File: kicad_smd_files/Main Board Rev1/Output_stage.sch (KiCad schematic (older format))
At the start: 41 parts, among them J10 OUTPUT B, J9 OUTPUT A, Q3 DMN10H170SK3-13, Q4 DMP6180SK3-13, Q5 DMN10H170SK3-13, Q6 DMN10H170SK3-13, Q7 DMP6180SK3-13, Q8 DMN10H170SK3-13, U7 LM358N, U8 LTC1661

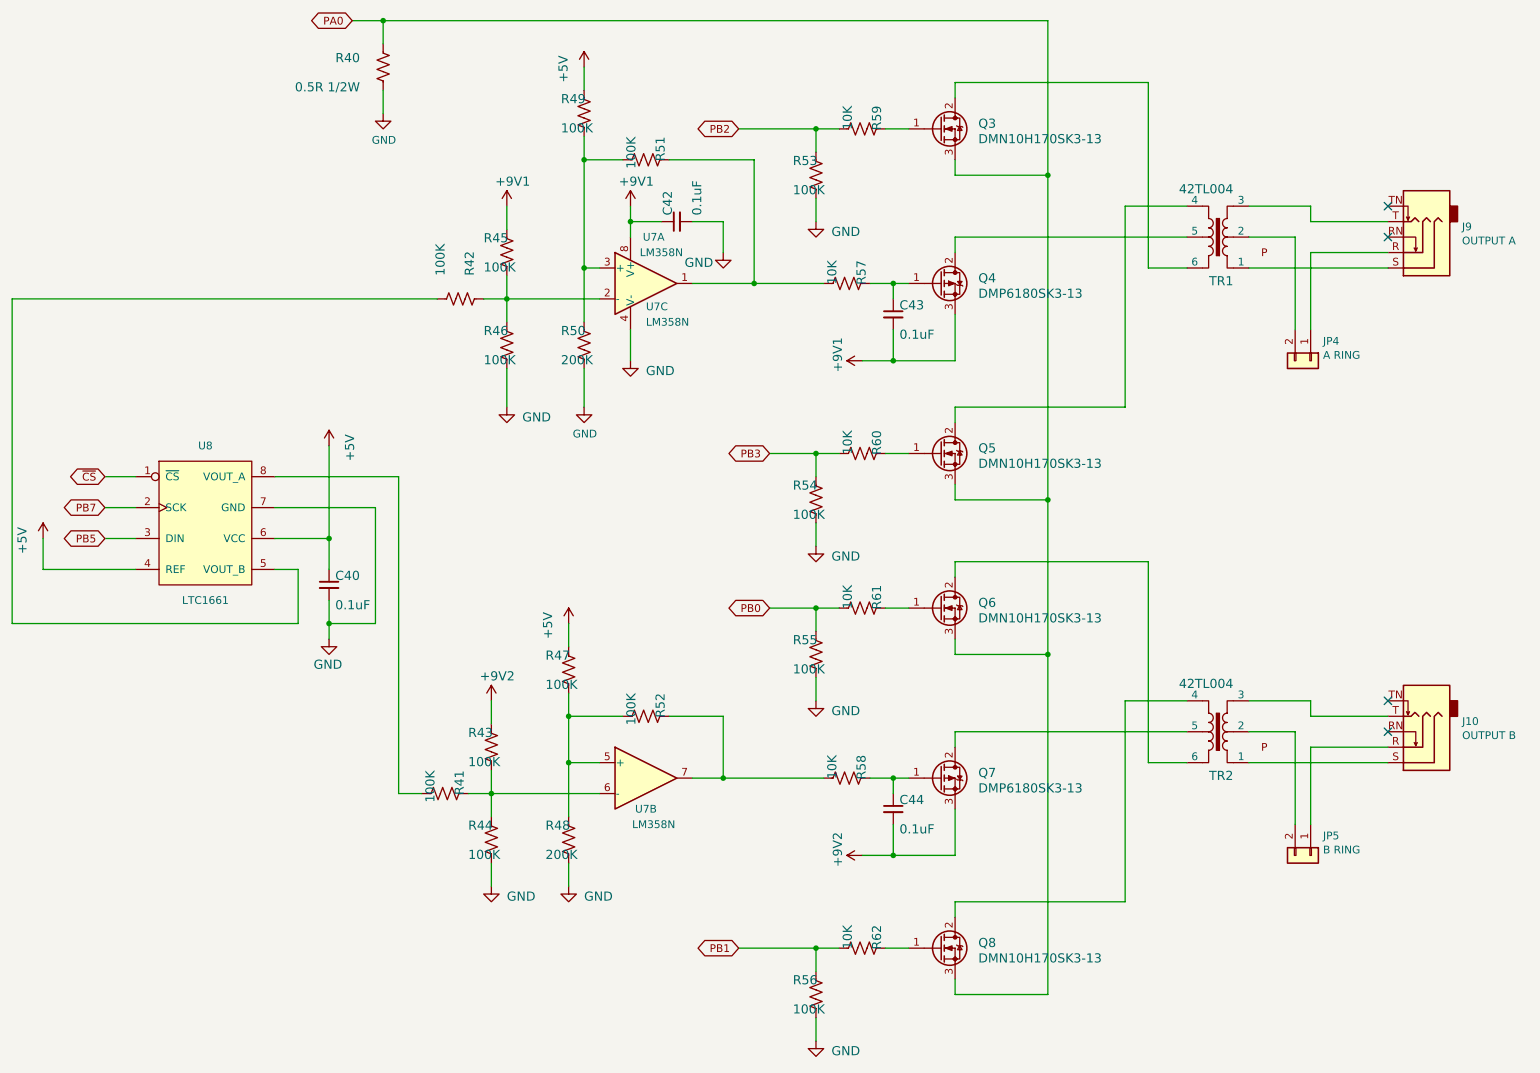
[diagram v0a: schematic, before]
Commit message: Smaller PCB, cheaper parts
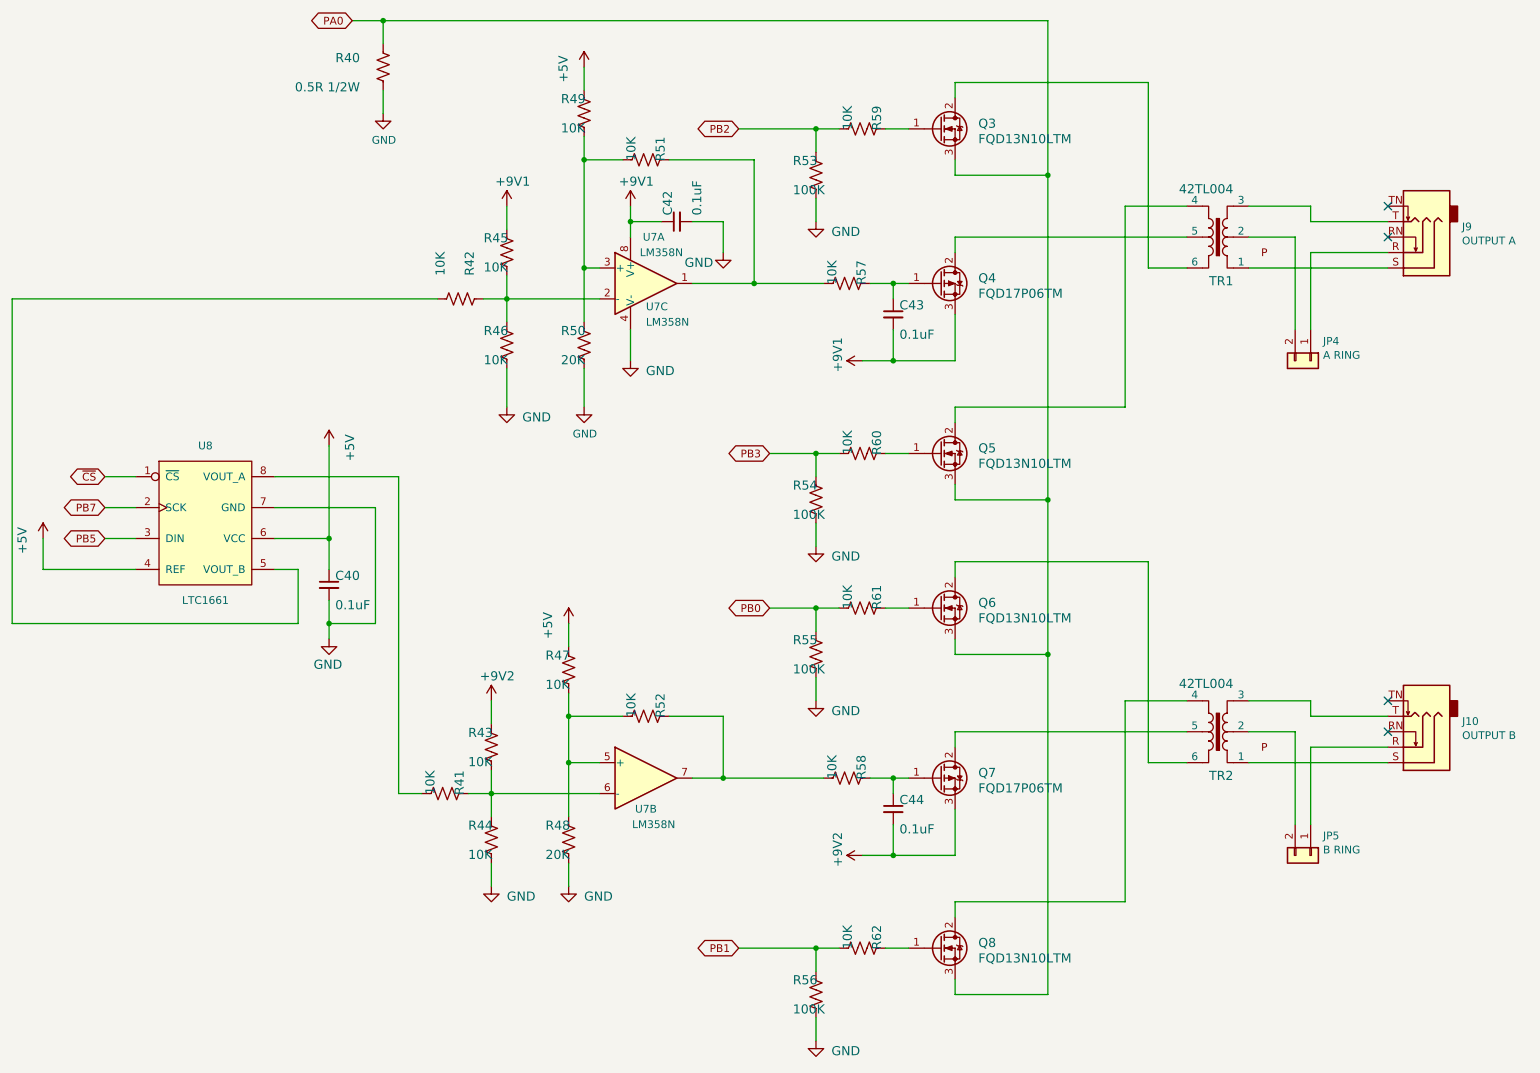
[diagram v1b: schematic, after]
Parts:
- C40, C42, C43, C44: Manufacturer_Name Murata -> Yageo; Manufacturer_Part_Number GCM155R71C104JA55D -> CC402KRX7R7BB104; Mouser Part Number 81-GCM155R71C104JA5D -> 603-CC402KRX7R7BB104
- Q3, Q5, Q6, Q8: value DMN10H170SK3-13 -> FQD13N10LTM; Manufacturer_Name Diodes Incorporated -> ON Semiconductor; Manufacturer_Part_Number DMN10H170SK3-13 -> FQD13N10LTM; Mouser Part Number 621-DMN10H170SK3-13 -> 512-FQD13N10LTM
- Q4, Q7: value DMP6180SK3-13 -> FQD17P06TM; Manufacturer_Name Diodes Incorporated -> ON Semiconductor; Manufacturer_Part_Number DMP6180SK3-13 -> FQD17P06TM; Mouser Part Number 621-DMP6180SK3-13 -> 512-FQD17P06TM
- R40: footprint Resistor_SMD:R_2010_5025Metric -> Resistor_SMD:R_1210_3225Metric; Manufacturer_Name Vishay -> Yageo; Manufacturer_Part_Number WSL2010R5000FEA -> RL1210FR070R5L; Mouser Part Number 71-WSL2010R5000FEA -> 603-RL1210FR070R5L
- R41, R42, R43, R44, R45, R46, R47, R49, R51, R52: value 100K -> 10K; footprint Resistor_SMD:R_0603_1608Metric -> Resistor_SMD:R_0402_1005Metric; Manufacturer_Name Panasonic -> Yageo; Manufacturer_Part_Number ERJ-PA3F1003V -> RC0402FR-0710KL; Mouser Part Number 667-ERJ-PA3F1003V -> 603-RC0402FR-0710KL
- R48, R50: value 200K -> 20K; footprint Resistor_SMD:R_0603_1608Metric -> Resistor_SMD:R_0402_1005Metric; Manufacturer_Name Panasonic -> Yageo; Manufacturer_Part_Number ERJ-PA3F2003V -> RC0402FR-0720KL; Mouser Part Number 667-ERJ-PA3F2003V -> 603-RC0402FR-0720KL
- R53, R54, R55, R56: footprint Resistor_SMD:R_0603_1608Metric -> Resistor_SMD:R_0402_1005Metric; Manufacturer_Name Panasonic -> Yageo; Manufacturer_Part_Number ERJ-PA3F1003V -> RC0402FR-07100KL; Mouser Part Number 667-ERJ-PA3F1003V -> 603-RC0402FR-07100KL
- R57, R58, R59, R60, R61, R62: footprint Resistor_SMD:R_0603_1608Metric -> Resistor_SMD:R_0402_1005Metric; Manufacturer_Name Panasonic -> Yageo; Manufacturer_Part_Number ERJ-PA3F1002V -> RC0402FR-0710KL; Mouser Part Number 667-ERJ-PA3F1002V -> 603-RC0402FR-0710KL
- U7: footprint Package_SO:SOIC-8_3.9x4.9mm_P1.27mm -> Package_SO:VSSOP-8_3.0x3.0mm_P0.65mm; Manufacturer_Part_Number LM358ADR -> LM358ADGKR; Mouser Part Number 595-LM358ADR -> 595-LM358ADGKR
